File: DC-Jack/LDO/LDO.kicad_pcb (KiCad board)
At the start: 4 copper layers, 32 x 83 mm, 32 parts, among them J1 Barrel_Jack_Switch, J2 Conn_01x03_Pin, J3 AudioJack2_Ground, J4 AudioJack2_Ground, J5 Conn_02x04_Odd_Even, J6 Conn_02x04_Odd_Even, U1 LM27762, U2 OPA1655

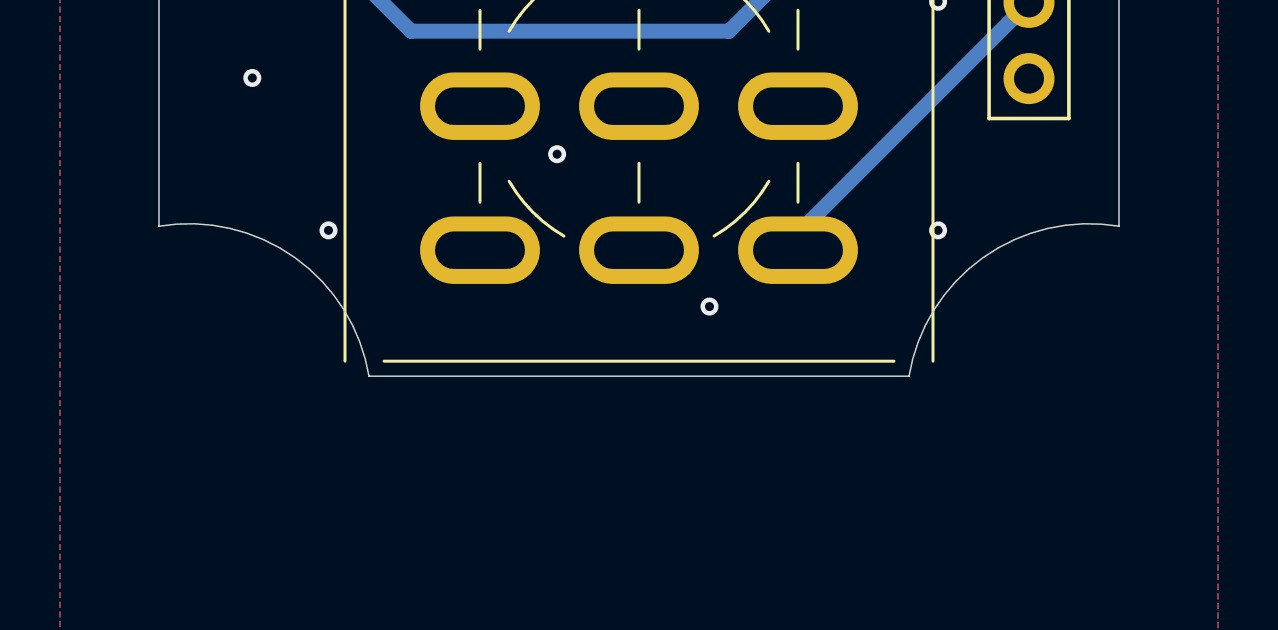
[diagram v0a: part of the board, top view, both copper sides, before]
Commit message: Do more edge cut fixups and update for new naming
This fixes all (?) the base boards to have the symmetric outline rather
than missing one mm at the bottom.

In the process it also ends up updating the file-name information inside
the kicad files that came about due to the renames.

Off to manufacturing to see if any of them work.

Signed-off-by: Linus Torvalds <torvalds@linux-foundation.org>
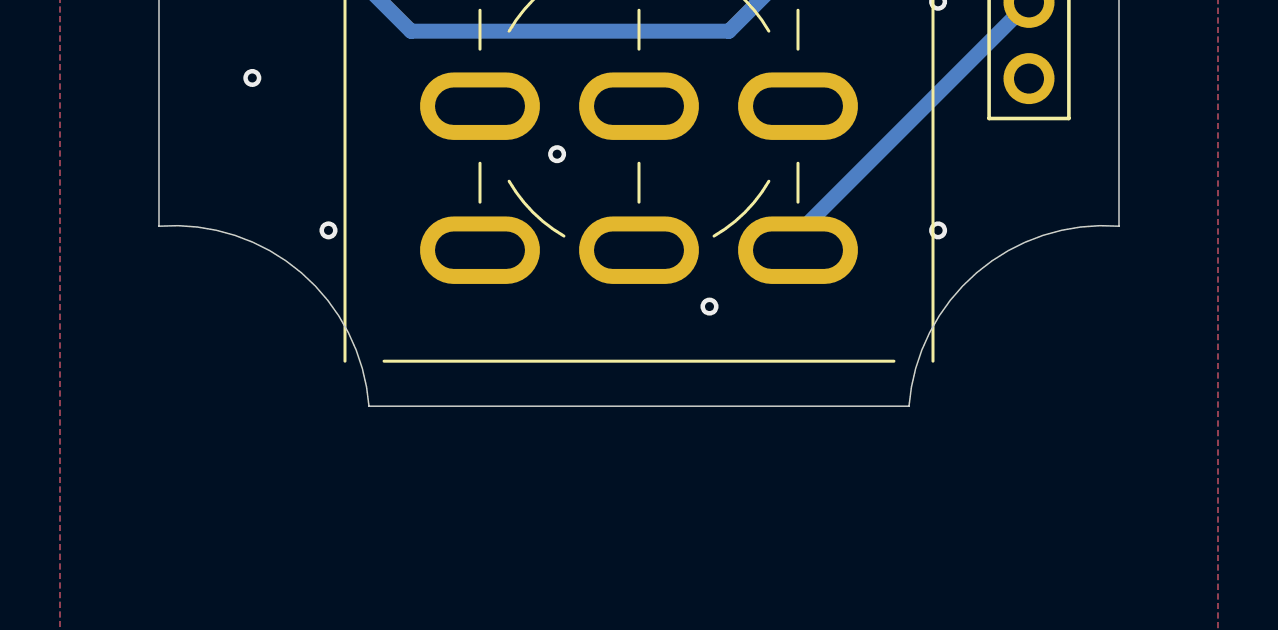
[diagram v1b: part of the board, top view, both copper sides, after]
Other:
- board size 32 x 83 mm -> 32 x 84 mm
